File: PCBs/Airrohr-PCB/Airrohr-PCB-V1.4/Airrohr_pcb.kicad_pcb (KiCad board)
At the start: 2 copper layers, 68.6 x 71.1 mm, 26 parts, among them J1 Conn_01x05, J10 Conn_01x04_Male, J11 RJ12, J12 RJ12, J2 Screw_Terminal_01x02, J3 Conn_01x02_Male, J4 Conn_01x04_Male, J5 Conn_01x05, J6 Conn_01x04_Male, J7 Conn_01x04_Male, J8 Conn_01x04_Male, J9 Conn_01x04_Male, U1 NodeMCU V3, U2 NodeMCU V2, U3 P82B715PN, U4 P82B715DR

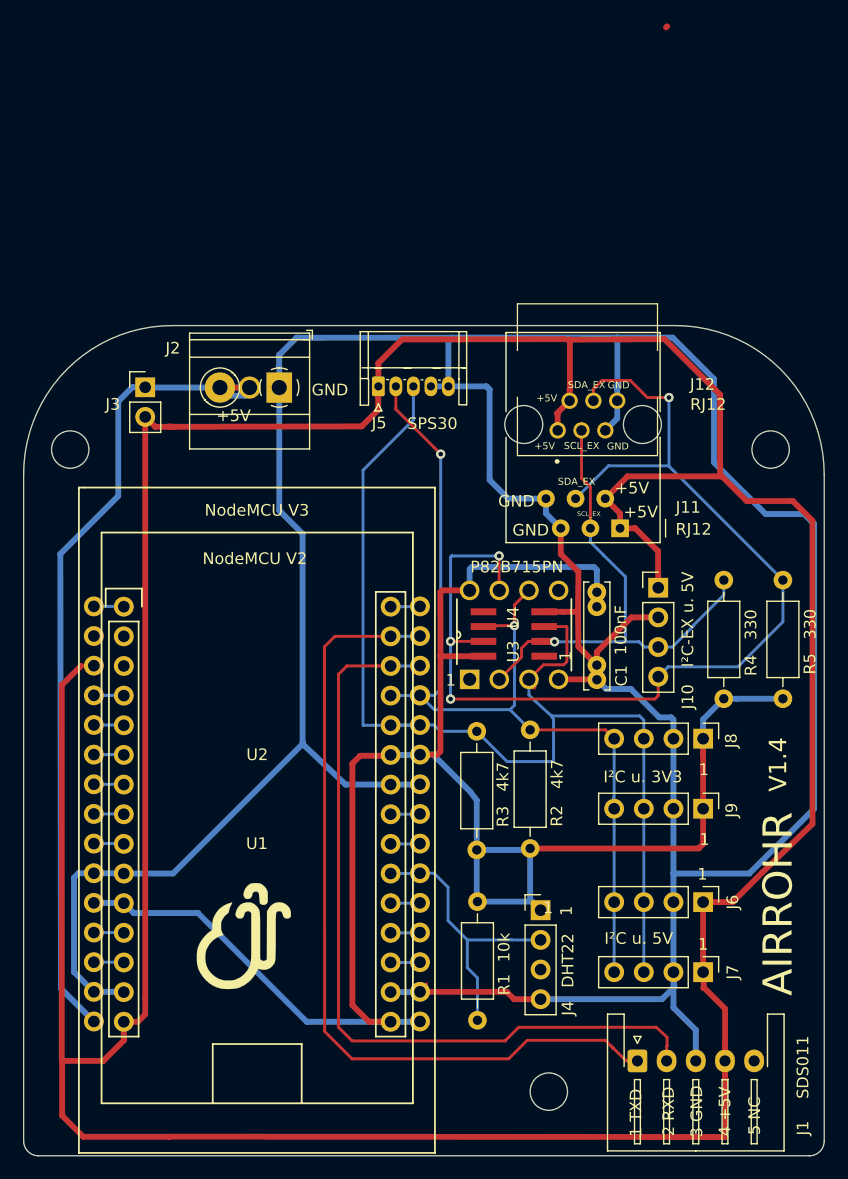
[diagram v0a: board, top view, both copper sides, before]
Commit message: Änderungen im Bestückungsdruck/change of silkscreen
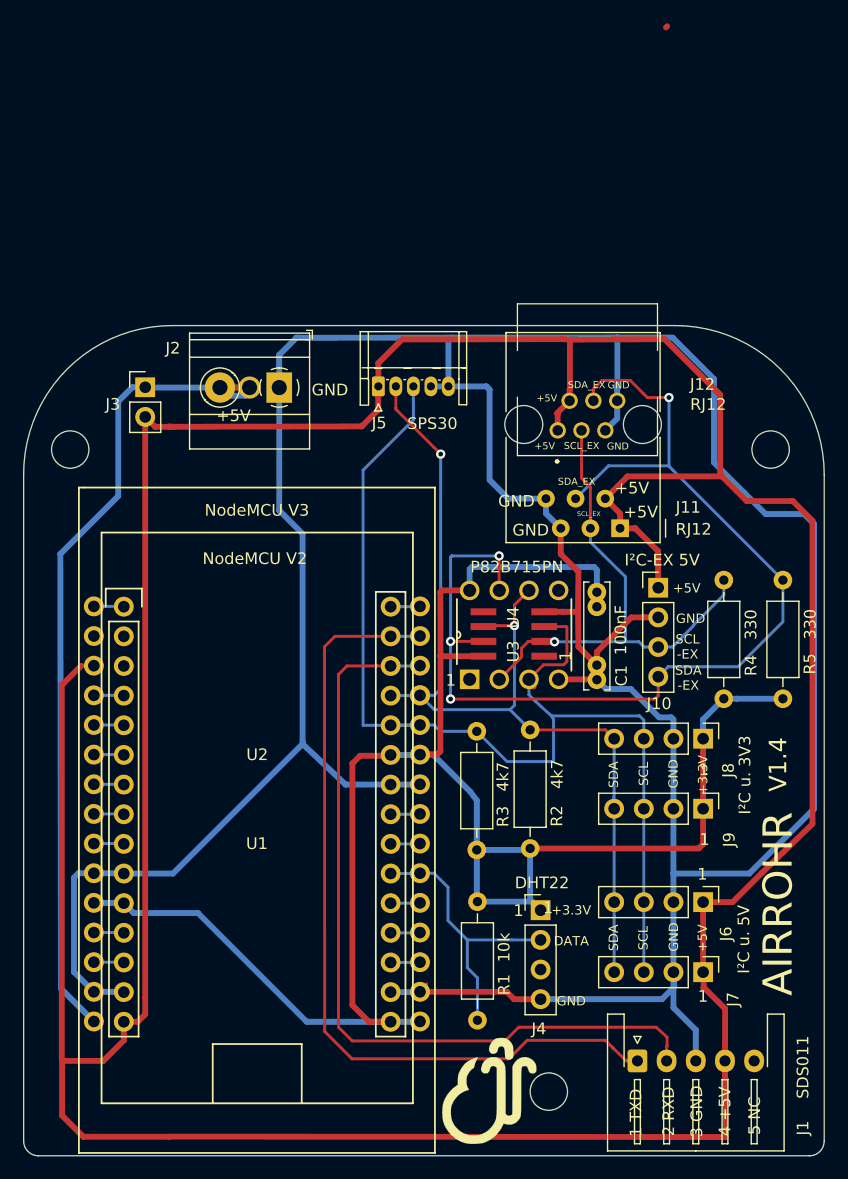
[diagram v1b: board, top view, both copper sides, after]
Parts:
- moved G*** 24.9 mm to (179.6, 83.3)
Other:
- board text added: "+3.3V"
- board text added: "DATA"
- board text added: "I²C-EX 5V"
- board text added: "SCL"
- board text added: "SCL -EX"
- board text added: "SDA"
- board text added: "SDA -EX"
- board text removed: "I²C-EX u. 5V"
